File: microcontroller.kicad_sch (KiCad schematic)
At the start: 41 parts, among them J1 TAG-10PIN, J2 USB4105-GF-A, U10 W25Q64JVXGIM, U2 W25Q64JVXGIM, U8 MIMXRT1061DVJ6B, U9 MKL02Z32VFG4, Y1 ABM8G-24.000MHZ-18-D2Y-T, Y2 ECS-_327-12_5-34B-TR

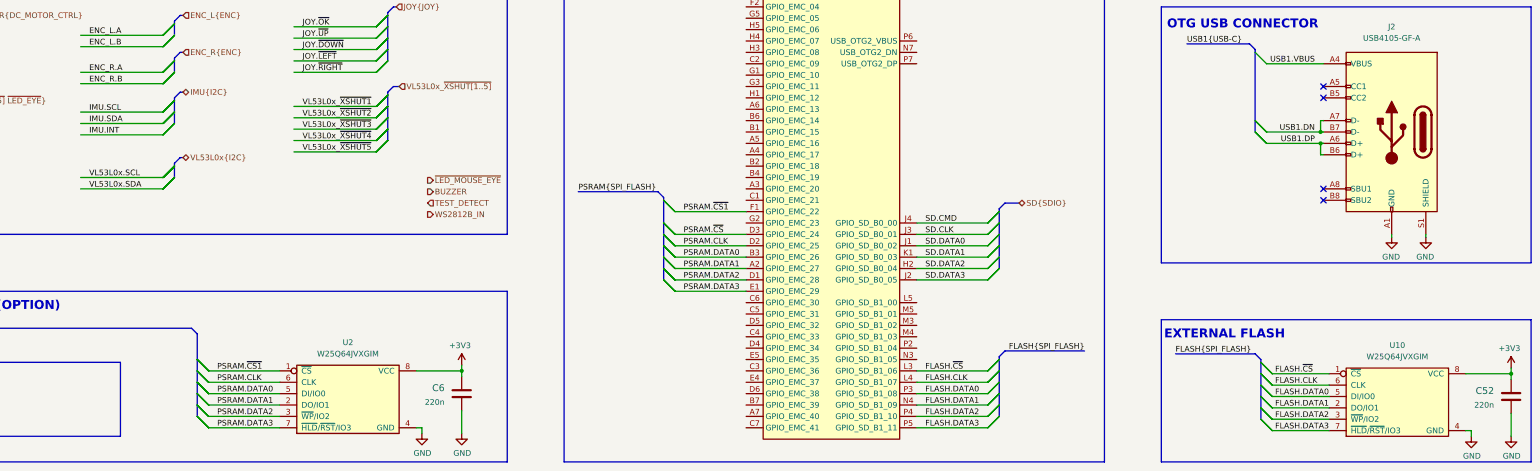
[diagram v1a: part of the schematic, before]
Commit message: Remove VLX wiring
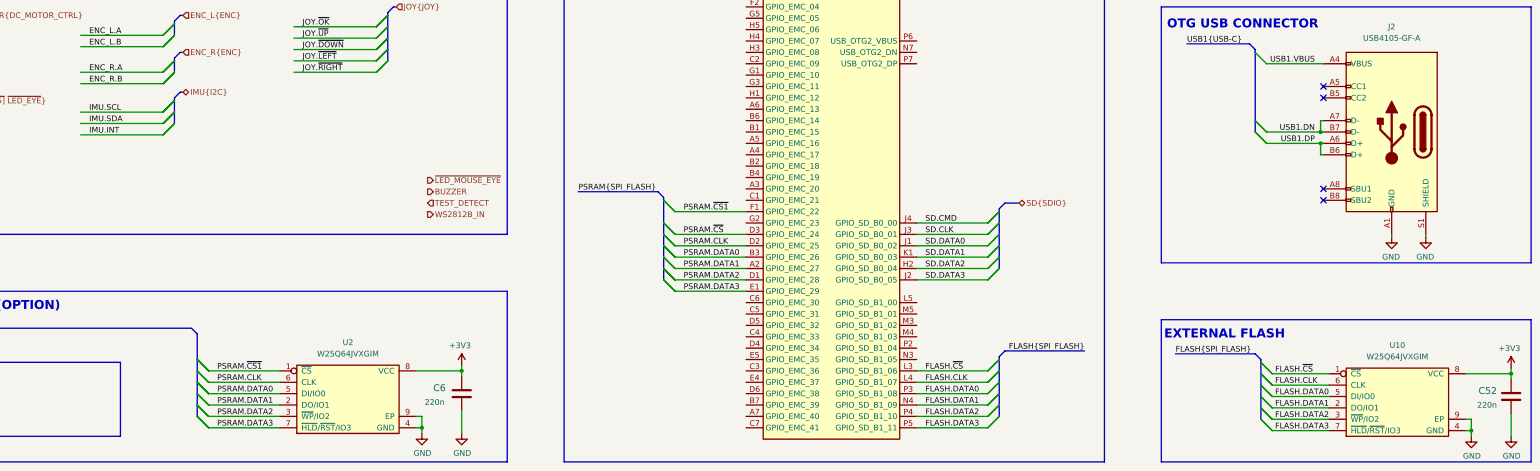
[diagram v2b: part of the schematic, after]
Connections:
- net GND: now also U10.9 (EP), U2.9 (EP)

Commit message: Loclib, cleanup
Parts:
- C27, C45, C48, C50: footprint antmicro-footprints:0402-cap -> synermycha-electronics-footprints:0402-cap; symbol antmicroCapacitors0402:C_10u_0402 -> synermycha-electronics:C_10u_0402
- C28, C34, C37, C38, C39, C41, C42, C43, C46, C51, C52, C6: footprint antmicro-footprints:0402-cap -> synermycha-electronics-footprints:0402-cap; symbol antmicroCapacitors0402:C_220n_0402 -> synermycha-electronics:C_220n_0402
- C29, C32: footprint antmicro-footprints:0402-cap -> synermycha-electronics-footprints:0402-cap; symbol antmicroCapacitors0402:C_12p_0402 -> synermycha-electronics:C_12p_0402
- C30, C33: footprint antmicro-footprints:0402-cap -> synermycha-electronics-footprints:0402-cap; symbol antmicroCapacitors0402:C_18p_0402 -> synermycha-electronics:C_18p_0402
- C31, C40, C44, C47, C49: footprint antmicro-footprints:0402-cap -> synermycha-electronics-footprints:0402-cap; symbol antmicroCapacitors0402:C_4u7_0402 -> synermycha-electronics:C_4u7_0402
- C35, C36: footprint antmicro-footprints:0402-cap -> synermycha-electronics-footprints:0402-cap; symbol antmicroCapacitors0402:C_10n_0402 -> synermycha-electronics:C_10n_0402
- FB1: footprint antmicro-footprints:0402-res -> synermycha-electronics-footprints:0402-res; symbol antmicroFerriteBeadsandChips:MPZ1005S121CT000 -> synermycha-electronics:MPZ1005S121CT000
- J1: footprint antmicro-footprints:TC2050-IDC-NL_2x05_Vertical -> synermycha-electronics-footprints:TC2050-IDC-NL_2x05_Vertical; symbol antmicroTestPoints:TAG-10PIN -> synermycha-electronics:TAG-10PIN
- J2: footprint antmicro-footprints:GCT_USB4105-GF-A -> synermycha-electronics-footprints:GCT_USB4105-GF-A; symbol antmicroUSBDVIHDMIConnectors:USB4105-GF-A -> synermycha-electronics:USB4105-GF-A
- L1: footprint antmicro-footprints:SRP2512A-1R0M -> synermycha-electronics-footprints:SRP2512A-1R0M; symbol antmicroFixedInductors:SRP2512A-4R7M -> synermycha-electronics:SRP2512A-4R7M
- R11: footprint antmicro-footprints:0402-res -> synermycha-electronics-footprints:0402-res; symbol antmicroResistors0402:R_100k_0402 -> synermycha-electronics:R_100k_0402
- R12: footprint antmicro-footprints:0402-res -> synermycha-electronics-footprints:0402-res; symbol antmicroResistors0402:R_2M0_0402 -> synermycha-electronics:R_2M0_0402
- TP13, TP14: footprint antmicro-footprints:Testpoint_smd_0_75mm -> synermycha-electronics-footprints:Testpoint_smd_0_75mm; symbol antmicroTestPoints:TP_SMD_0_75MM -> synermycha-electronics:TP_SMD_0_75MM
- U10, U2: footprint antmicro-footprints:WSON-8-1EP_4x4mm_P0.8mm_EP2.6x3mm -> synermycha-electronics-footprints:WSON-8-1EP_4x4mm_P0.8mm_EP2.6x3mm; symbol antmicroMemory:W25Q64JVXGIM -> synermycha-electronics:W25Q64JVXGIM
- U8: footprint antmicro-footprints:NXP_MAPBGA-196_14x14_12.0x12.0mm -> synermycha-electronics-footprints:NXP_MAPBGA-196_14x14_12.0x12.0mm; symbol antmicroMicrocontrollers:MIMXRT1061DVJ6B -> synermycha-electronics:MIMXRT1061DVJ6B
- U9: footprint antmicro-footprints:VQFN-16-1EP_3x3mm -> synermycha-electronics-footprints:VQFN-16-1EP_3x3mm; symbol antmicroMicrocontrollers:MKL02Z32VFG4 -> synermycha-electronics:MKL02Z32VFG4
- Y1: footprint antmicro-footprints:KX-7 -> synermycha-electronics-footprints:KX-7; symbol antmicroCrystals:ABM8G-24.000MHZ-18-D2Y-T -> synermycha-electronics:ABM8G-24.000MHZ-18-D2Y-T
- Y2: footprint antmicro-footprints:SMD-2_3.2x1.5mm -> synermycha-electronics-footprints:SMD-2_3.2x1.5mm; symbol antmicroCrystals:ECS-_327-12_5-34B-TR -> synermycha-electronics:ECS-_327-12_5-34B-TR
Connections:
- net +3V3: no longer U2.8 (VCC), U8.E6 (NVCC_EMP), U8.E9 (NVCC_GPIO), U8.F10 (NVCC_GPIO), U8.F5 (NVCC_EMC), U8.J10 (NVCC_GPIO), U8.J6 (NVCC_SD0), U8.K5 (NVCC_SD1), U8.M9 (VDD_SNVS_IN), U8.N14 (VDD_ADC), U8.P12 (VDD_HIGH_IN)
- net BOOT_MODE0: no longer U8.F11 (GPIO_AD_B0_04)
- net BOOT_MODE1: no longer U8.G14 (GPIO_AD_B0_05)
- net BT_CFG9: no longer U8.D10 (GPIO_B0_13)
- net GND: no longer U2.4 (GND), U2.9 (EP), U8.A1 (VSS), U8.A14 (VSS), U8.B10 (VSS), U8.B5 (VSS), U8.E13 (VSS), U8.E2 (VSS), U8.G7 (VSS), U8.G8 (VSS), U8.H7 (VSS), U8.H8 (VSS), U8.J7 (VSS), U8.J8 (VSS), U8.K13 (VSS), U8.K2 (VSS), U8.K6 (TEST_MODE), U8.K9 (NGND_KEL0), U8.L9 (VSS), U8.N1 (DCDC_GND), U8.N2 (DCDC_GND), U8.N5 (VSS), U8.N8 (VSS), U8.P1 (VSS), U8.P14 (VSS)
- net JTAG.TCK: no longer U8.F12 (GPIO_AD_B0_07)
- net JTAG.TDI: no longer U8.F14 (GPIO_AD_B0_09)
- net JTAG.TDO: no longer U8.G13 (GPIO_AD_B0_10)
- net JTAG.TMS: no longer U8.E14 (GPIO_AD_B0_06)
- net JTAG_MOD: no longer U8.F13 (GPIO_AD_B0_08)
- net MCU_DCDC_IN: no longer U8.K4 (DCDC_IN_Q), U8.L1 (DCDC_IN), U8.L2 (DCDC_IN)
- net MCU_DCDC_PSWITCH: no longer U8.G10 (GPIO_AD_B0_11), U8.K3 (DCDC_PSWITCH)
- net MCU_NVCC_PLL: no longer U8.P10 (NVCC_PLL)
- net MCU_ONOFF: no longer U8.M6 (ONOFF)
- net MCU_PMIC_ON_REQ: no longer U8.K7 (PMIC_ON_REQ)
- net MCU_PMIC_STBT_REQ: no longer U8.L7 (PMIC_STBY_REQ)
- net MCU_POR_B: no longer U8.M7 (POR_B)
- net MCU_VDD_HIGH_CAP: no longer U8.P8 (VDD_HIGH_CAP)
- net MCU_VDD_SNVS_CAP: no longer U8.M10 (SNVS_CAP)
- net MCU_VDD_USB_VCAP: no longer U8.K8 (VDD_USB_CAP)
- net MCU_WAKEUP: no longer U8.L6 (WAKEUP)
- net PSRAM.CLK: no longer U2.6 (CLK)
- net PSRAM.DATA0: no longer U2.5 (DI/IO0)
- net PSRAM.DATA1: no longer U2.2 (DO/IO1)
- net PSRAM.DATA2: no longer U2.3 (~{WP}/IO2)
- net PSRAM.DATA3: no longer U2.7 (~{HLD}/~{RST}/IO3)
- net PSRAM.~{CS1}: no longer U2.1 (~{CS})
- net SOC_DCDD_LP: no longer U8.M1 (DCDC_LP), U8.M2 (DCDC_LP)
- net SOC_RTC_XTALI: no longer U8.N9 (RTC_XTALI)
- net SOC_RTC_XTALO: no longer U8.P9 (RTC_XTALO)
- net SOC_VDD_CORE: no longer U8.F6 (VDD_SOC_IN), U8.F7 (VDD_SOC_IN), U8.F8 (VDD_SOC_IN), U8.F9 (VDD_SOC_IN), U8.G6 (VDD_SOC_IN), U8.G9 (VDD_SOC_IN), U8.H6 (VDD_SOC_IN), U8.H9 (VDD_SOC_IN), U8.J5 (DCDC_SENSE), U8.J9 (VDD_SOC_IN)
- net SOC_XTALI: no longer U8.P11 (XTALI)
- net SOC_XTALO: no longer U8.N11 (XTALO)
